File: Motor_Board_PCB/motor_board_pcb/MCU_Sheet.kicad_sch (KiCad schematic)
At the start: 39 parts

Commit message: Motor Board Initial Layout
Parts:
- removed SW?: SW_Push, Button_Switch_SMD:SW_Push_1P1T_NO_6x6mm_H9.5mm, symbol Switch:SW_Push
- removed TP? (x3): TestPoint, TestPoint:TestPoint_Pad_D1.0mm, symbol Connector:TestPoint
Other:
- moved on the sheet: TP?

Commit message: Meeting layout updates
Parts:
- added R7 (x3): 0, Resistor_SMD:R_0402_1005Metric, symbol Device:R
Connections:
- net D10: now also R7.1; no longer U?.37 (GTIOC3B/P112)
- net D11: now also R7.1; no longer U?.34 (CTX0/TDO/SWO/GTIOC1A/P109)
- net D13: now also R7.1; no longer U?.36 (GTIOC3A/P111)
- new net: R7.2, U?.34 (CTX0/TDO/SWO/GTIOC1A/P109)
- new net: R7.2, U?.36 (GTIOC3A/P111)
- new net: R7.2, U?.37 (GTIOC3B/P112)
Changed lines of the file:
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@@
-    (stroke (width 0) (type default))
-  )
-  (wire (pts (xy 190.5 87.63) (xy 208.28 87.63))
     (stroke (width 0) (type default))
   )
@@
     (stroke (width 0) (type default))
   )
+  (wire (pts (xy 198.12 92.71) (xy 215.9 92.71))
+    (stroke (width 0) (type default))
+  )
   (wire (pts (xy 115.57 74.93) (xy 119.38 74.93))
     (stroke (width 0) (type default))
@@
     (stroke (width 0) (type default))
   )
-  (wire (pts (xy 190.5 90.17) (xy 208.28 90.17))
+  (wire (pts (xy 198.12 85.09) (xy 215.9 85.09))
     (stroke (width 0) (type default))
   )
@@
     (stroke (width 0) (type default))
   )
-  (wire (pts (xy 190.5 85.09) (xy 208.28 85.09))
-    (stroke (width 0) (type default))
-  )
   (wire (pts (xy 233.68 102.87) (xy 237.49 102.87))
     (stroke (width 0) (type default))
@@
     (stroke (width 0) (type default))
   )
+  (wire (pts (xy 198.12 90.17) (xy 215.9 90.17))
+    (stroke (width 0) (type default))
+  )
   (wire (pts (xy 119.38 49.53) (xy 105.41 49.53))
     (stroke (width 0) (type default))
@@
     (stroke (width 0) (type default))
   )
-  (wire (pts (xy 190.5 92.71) (xy 208.28 92.71))
-    (stroke (width 0) (type default))
-  )
   (wire (pts (xy 165.1 168.91) (xy 165.1 166.37))
     (stroke (width 0) (type default))
   )
   (wire (pts (xy 73.66 96.52) (xy 73.66 97.79))
+    (stroke (width 0) (type default))
+  )
+  (wire (pts (xy 190.5 87.63) (xy 215.9 87.63))
     (stroke (width 0) (type default))
   )
@@
     (effects (font (size 1.27 1.27)) (justify left bottom))
   )
-  (label "P109_SCI9_TXD" (at 191.77 85.09 0) (fields_autoplaced)
+  (label "P109_SCI9_TXD" (at 201.93 85.09 0) (fields_autoplaced)
     (effects (font (size 1.27 1.27)) (justify left bottom))
   )
@@
     (effects (font (size 1.27 1.27)) (justify left bottom))
   )
-  (label "P111_GPT3_A" (at 191.77 90.17 0) (fields_autoplaced)
+  (label "P111_GPT3_A" (at 201.93 90.17 0) (fields_autoplaced)
     (effects (font (size 1.27 1.27)) (justify left bottom))
   )
@@
     (effects (font (size 1.27 1.27)) (justify left bottom))
   )
-  (label "P112_GPT3_B" (at 191.77 92.71 0) (fields_autoplaced)
+  (label "P112_GPT3_B" (at 201.93 92.71 0) (fields_autoplaced)
     (effects (font (size 1.27 1.27)) (justify left bottom))
   )
@@
     (effects (font (size 1.27 1.27)) (justify left bottom))
   )
-  (label "P110_SCI9_RXD" (at 191.77 87.63 0) (fields_autoplaced)
+  (label "P110_SCI9_RXD" (at 201.93 87.63 0) (fields_autoplaced)
     (effects (font (size 1.27 1.27)) (justify left bottom))
   )
@@
     )
   )
-  (global_label "D11" (shape input) (at 208.28 85.09 0) (fields_autoplaced)
+  (global_label "D11" (shape input) (at 215.9 85.09 0) (fields_autoplaced)
     (effects (font (size 1.27 1.27)) (justify left))
-    (property "Intersheetrefs" "${INTERSHEET_REFS}" (at 214.9542 85.09 0)
+    (property "Intersheetrefs" "${INTERSHEET_REFS}" (at 222.5742 85.09 0)
       (effects (font (size 1.27 1.27)) (justify left) hide)
     )
@@
     )
   )
-  (global_label "D13" (shape input) (at 208.28 90.17 0) (fields_autoplaced)
+  (global_label "D13" (shape input) (at 215.9 90.17 0) (fields_autoplaced)
     (effects (font (size 1.27 1.27)) (justify left))
-    (property "Intersheetrefs" "${INTERSHEET_REFS}" (at 214.9542 90.17 0)
+    (property "Intersheetrefs" "${INTERSHEET_REFS}" (at 222.5742 90.17 0)
       (effects (font (size 1.27 1.27)) (justify left) hide)
     )
@@
     )
   )
-  (global_label "D10" (shape input) (at 208.28 92.71 0) (fields_autoplaced)
+  (global_label "D10" (shape input) (at 215.9 92.71 0) (fields_autoplaced)
     (effects (font (size 1.27 1.27)) (justify left))
-    (property "Intersheetrefs" "${INTERSHEET_REFS}" (at 214.9542 92.71 0)
+    (property "Intersheetrefs" "${INTERSHEET_REFS}" (at 222.5742 92.71 0)
       (effects (font (size 1.27 1.27)) (justify left) hide)
     )
@@
     )
   )
-  (global_label "D12" (shape input) (at 208.28 87.63 0) (fields_autoplaced)
+  (global_label "D12" (shape input) (at 215.9 87.63 0) (fields_autoplaced)
     (effects (font (size 1.27 1.27)) (justify left))
-    (property "Intersheetrefs" "${INTERSHEET_REFS}" (at 214.9542 87.63 0)
+    (property "Intersheetrefs" "${INTERSHEET_REFS}" (at 222.5742 87.63 0)
       (effects (font (size 1.27 1.27)) (justify left) hide)
     )
@@
         (path "/4ad82a24-c992-45c9-b523-12e12bcd6ced/677bf49c-46b9-40dd-b186-394fb8d84e12"
           (reference "#PWR019") (unit 1)
+        )
+      )
+    )
+  )
+  (symbol (lib_id "Device:R") (at 194.31 85.09 270) (unit 1)
+    (in_bom yes) (on_board yes) (dnp no)
+    (property "Reference" "R7" (at 199.39 86.36 90)
+      (effects (font (size 1.27 1.27)))
+    )
+    (property "Value" "0" (at 190.5 83.82 90)
+      (effects (font (size 1.27 1.27)))
+    )
+    (property "Footprint" "Resistor_SMD:R_0402_1005Metric" (at 194.31 83.312 90)
+      (effects (font (size 1.27 1.27)) hide)
+    )
+    (property "Datasheet" "~" (at 194.31 85.09 0)
+      (effects (font (size 1.27 1.27)) hide)
+    )
+    (pin "1")
+    (pin "2")
+    (instances
+      (project "central_hub"
+        (path "/0d9ec66e-0fbf-4d12-9b83-adf78971a00b/a9a7affa-d8a7-4dcd-8fe3-0de6a2b29bd6"
+          (reference "R7") (unit 1)
+        )
+        (path "/0d9ec66e-0fbf-4d12-9b83-adf78971a00b/4fb60496-ee10-4e45-a75e-a49c2c8afc68"
+          (reference "R35") (unit 1)
+        )
+      )
+      (project "motor_board_pcb"
+        (path "/4ad82a24-c992-45c9-b523-12e12bcd6ced"
+          (reference "R?") (unit 1)
+        )
+        (path "/4ad82a24-c992-45c9-b523-12e12bcd6ced/63c66207-e5d4-4f6f-af8f-451675dc3930"
+          (reference "R16") (unit 1)
+        )
+        (path "/4ad82a24-c992-45c9-b523-12e12bcd6ced/677bf49c-46b9-40dd-b186-394fb8d84e12"
+          (reference "R7") (unit 1)
         )
       )
@@
     )
   )
+  (symbol (lib_id "Device:R") (at 194.31 92.71 270) (unit 1)
+    (in_bom yes) (on_board yes) (dnp no)
+    (property "Reference" "R7" (at 199.39 93.98 90)
+      (effects (font (size 1.27 1.27)))
+    )
+    (property "Value" "0" (at 190.5 91.44 90)
+      (effects (font (size 1.27 1.27)))
+    )
+    (property "Footprint" "Resistor_SMD:R_0402_1005Metric" (at 194.31 90.932 90)
+      (effects (font (size 1.27 1.27)) hide)
+    )
+    (property "Datasheet" "~" (at 194.31 92.71 0)
+      (effects (font (size 1.27 1.27)) hide)
+    )
+    (pin "1")
+    (pin "2")
+    (instances
+      (project "central_hub"
+        (path "/0d9ec66e-0fbf-4d12-9b83-adf78971a00b/a9a7affa-d8a7-4dcd-8fe3-0de6a2b29bd6"
+          (reference "R7") (unit 1)
+        )
+        (path "/0d9ec66e-0fbf-4d12-9b83-adf78971a00b/4fb60496-ee10-4e45-a75e-a49c2c8afc68"
+          (reference "R35") (unit 1)
+        )
+      )
+      (project "motor_board_pcb"
+        (path "/4ad82a24-c992-45c9-b523-12e12bcd6ced"
+          (reference "R?") (unit 1)
+        )
+        (path "/4ad82a24-c992-45c9-b523-12e12bcd6ced/63c66207-e5d4-4f6f-af8f-451675dc3930"
+          (reference "R16") (unit 1)
+        )
+        (path "/4ad82a24-c992-45c9-b523-12e12bcd6ced/677bf49c-46b9-40dd-b186-394fb8d84e12"
+          (reference "R35") (unit 1)
+        )
+      )
+    )
+  )
   (symbol (lib_id "Device:C") (at 80.01 52.07 90) (unit 1)
     (in_bom yes) (on_board yes) (dnp no) (fields_autoplaced)
@@
         )
       )
+    )
+  )
+  (symbol (lib_id "Device:R") (at 194.31 90.17 270) (unit 1)
+    (in_bom yes) (on_board yes) (dnp no)
+    (property "Reference" "R7" (at 199.39 91.44 90)
+      (effects (font (size 1.27 1.27)))
+    )
+    (property "Value" "0" (at 190.5 88.9 90)
+      (effects (font (size 1.27 1.27)))
+    )
+    (property "Footprint" "Resistor_SMD:R_0402_1005Metric" (at 194.31 88.392 90)
+      (effects (font (size 1.27 1.27)) hide)
+    )
+    (property "Datasheet" "~" (at 194.31 90.17 0)
+      (effects (font (size 1.27 1.27)) hide)
+    )
+    (pin "1")
+    (pin "2")
+    (instances
+      (project "central_hub"
+        (path "/0d9ec66e-0fbf-4d12-9b83-adf78971a00b/a9a7affa-d8a7-4dcd-8fe3-0de6a2b29bd6"
+          (reference "R7") (unit 1)
+        )
+        (path "/0d9ec66e-0fbf-4d12-9b83-adf78971a00b/4fb60496-ee10-4e45-a75e-a49c2c8afc68"
+          (reference "R35") (unit 1)
+        )
+      )
+      (project "motor_board_pcb"
+        (path "/4ad82a24-c992-45c9-b523-12e12bcd6ced"
+          (reference "R?") (unit 1)
+        )
+        (path "/4ad82a24-c992-45c9-b523-12e12bcd6ced/63c66207-e5d4-4f6f-af8f-451675dc3930"
+          (reference "R16") (unit 1)
+        )
+        (path "/4ad82a24-c992-45c9-b523-12e12bcd6ced/677bf49c-46b9-40dd-b186-394fb8d84e12"
+          (reference "R34") (unit 1)
+        )
+      )

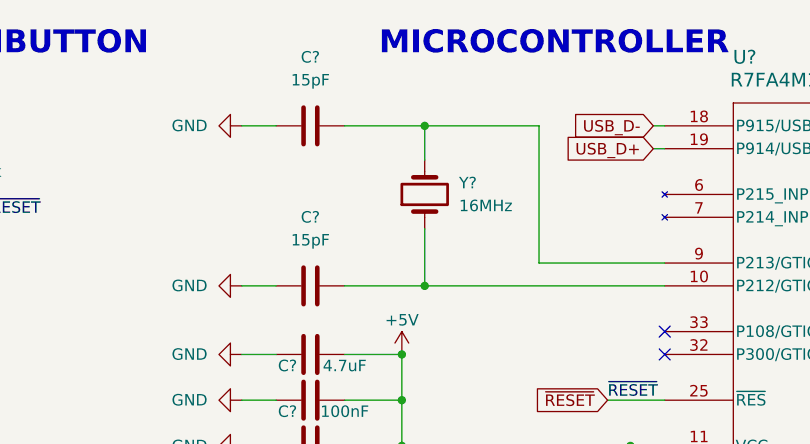
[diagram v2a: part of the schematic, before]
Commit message: Kim changes + GND pour + TearDrops + Oscillator changes
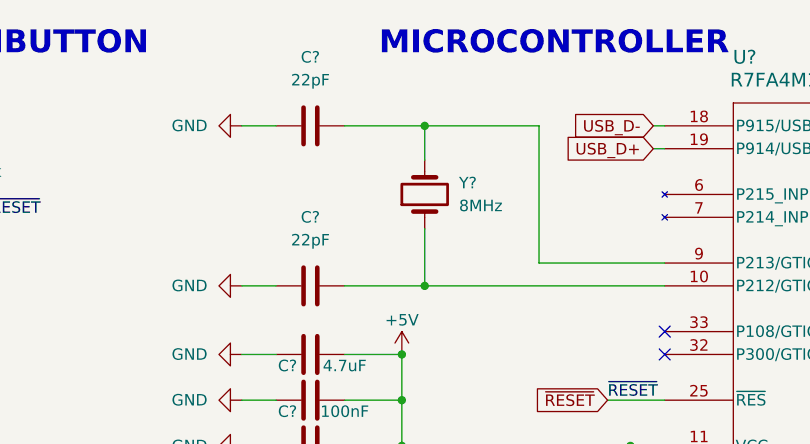
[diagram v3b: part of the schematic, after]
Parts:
- C? (x2): value 15pF -> 22pF
- Y?: value 16MHz -> 8MHz
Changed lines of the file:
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@@
       (effects (font (size 1.27 1.27)))
     )
-    (property "Value" "15pF" (at 80.01 29.21 90)
+    (property "Value" "22pF" (at 80.01 29.21 90)
       (effects (font (size 1.27 1.27)))
     )
@@
       (effects (font (size 1.27 1.27)) (justify right))
     )
-    (property "Value" "16MHz" (at 96.52 43.18 90)
+    (property "Value" "8MHz" (at 96.52 43.18 90)
       (effects (font (size 1.27 1.27)) (justify right))
     )
@@
       (effects (font (size 1.27 1.27)))
     )
-    (property "Value" "15pF" (at 80.01 46.99 90)
-      (effects (font (size 1.27 1.27)))
-    )
+    (property "Value" "22pF" (at 80.01 46.99 90)
+      (effects (font (size 1.27 1.27)))
+    )

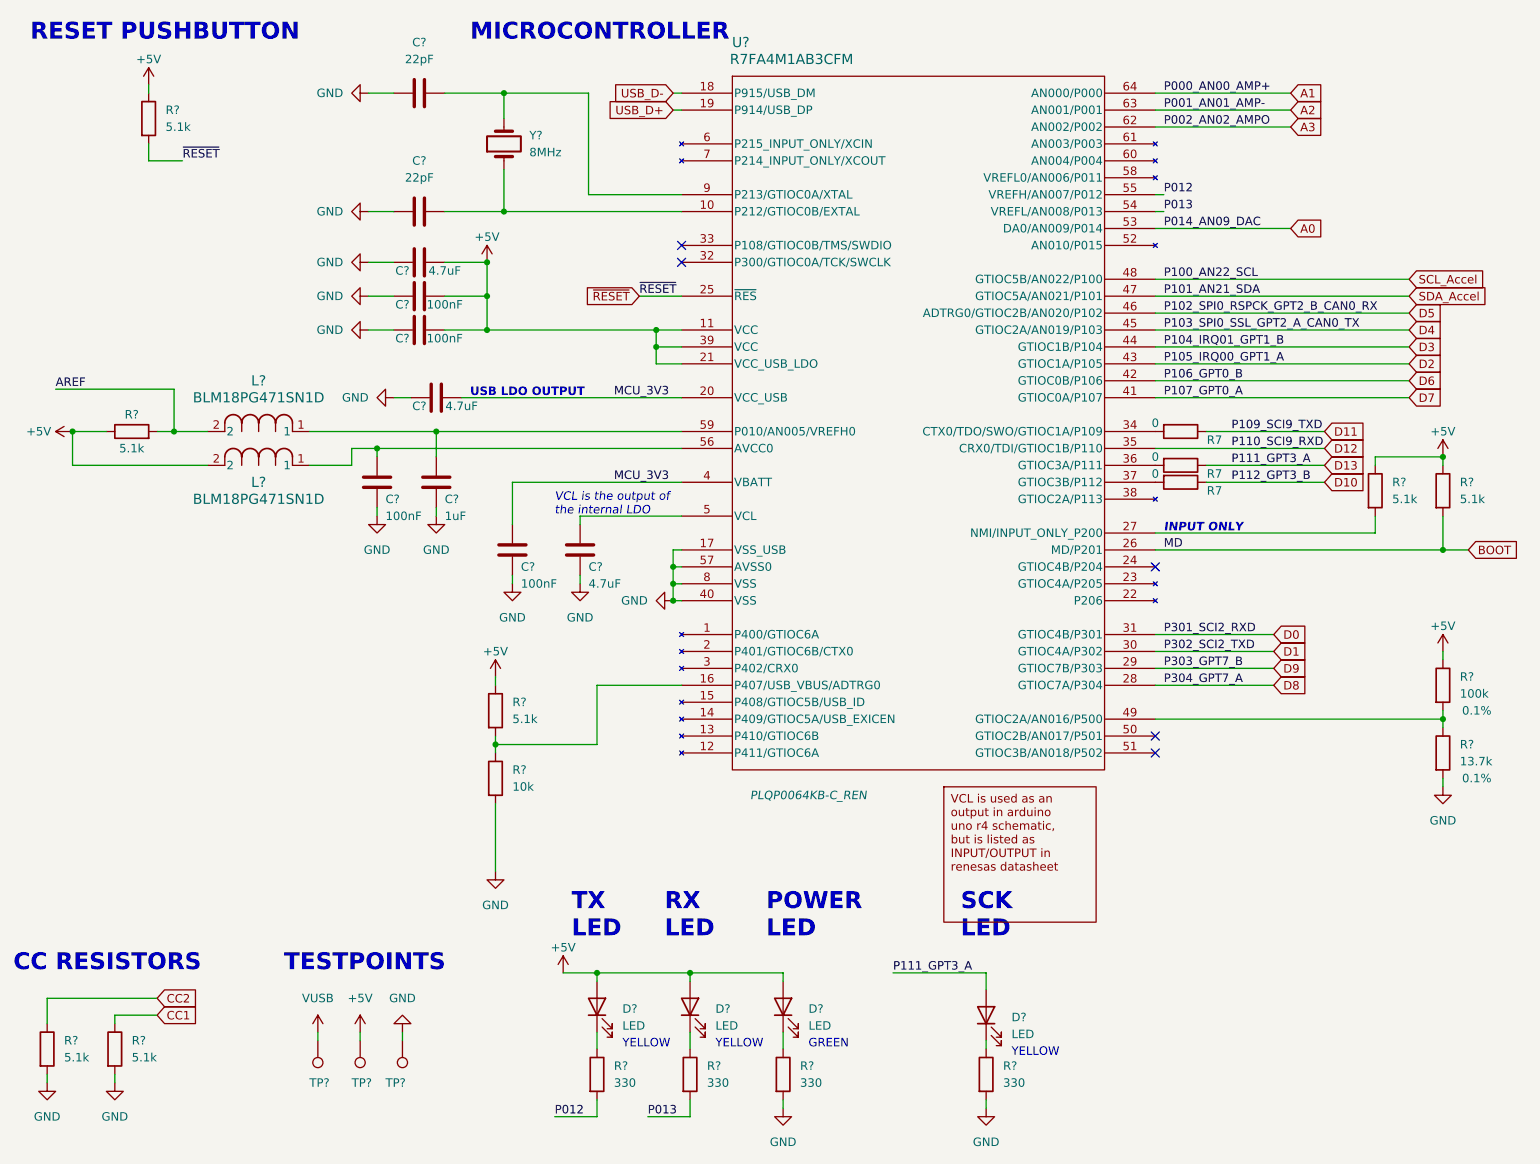
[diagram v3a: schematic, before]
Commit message: - added footprint labels to schematic symbols
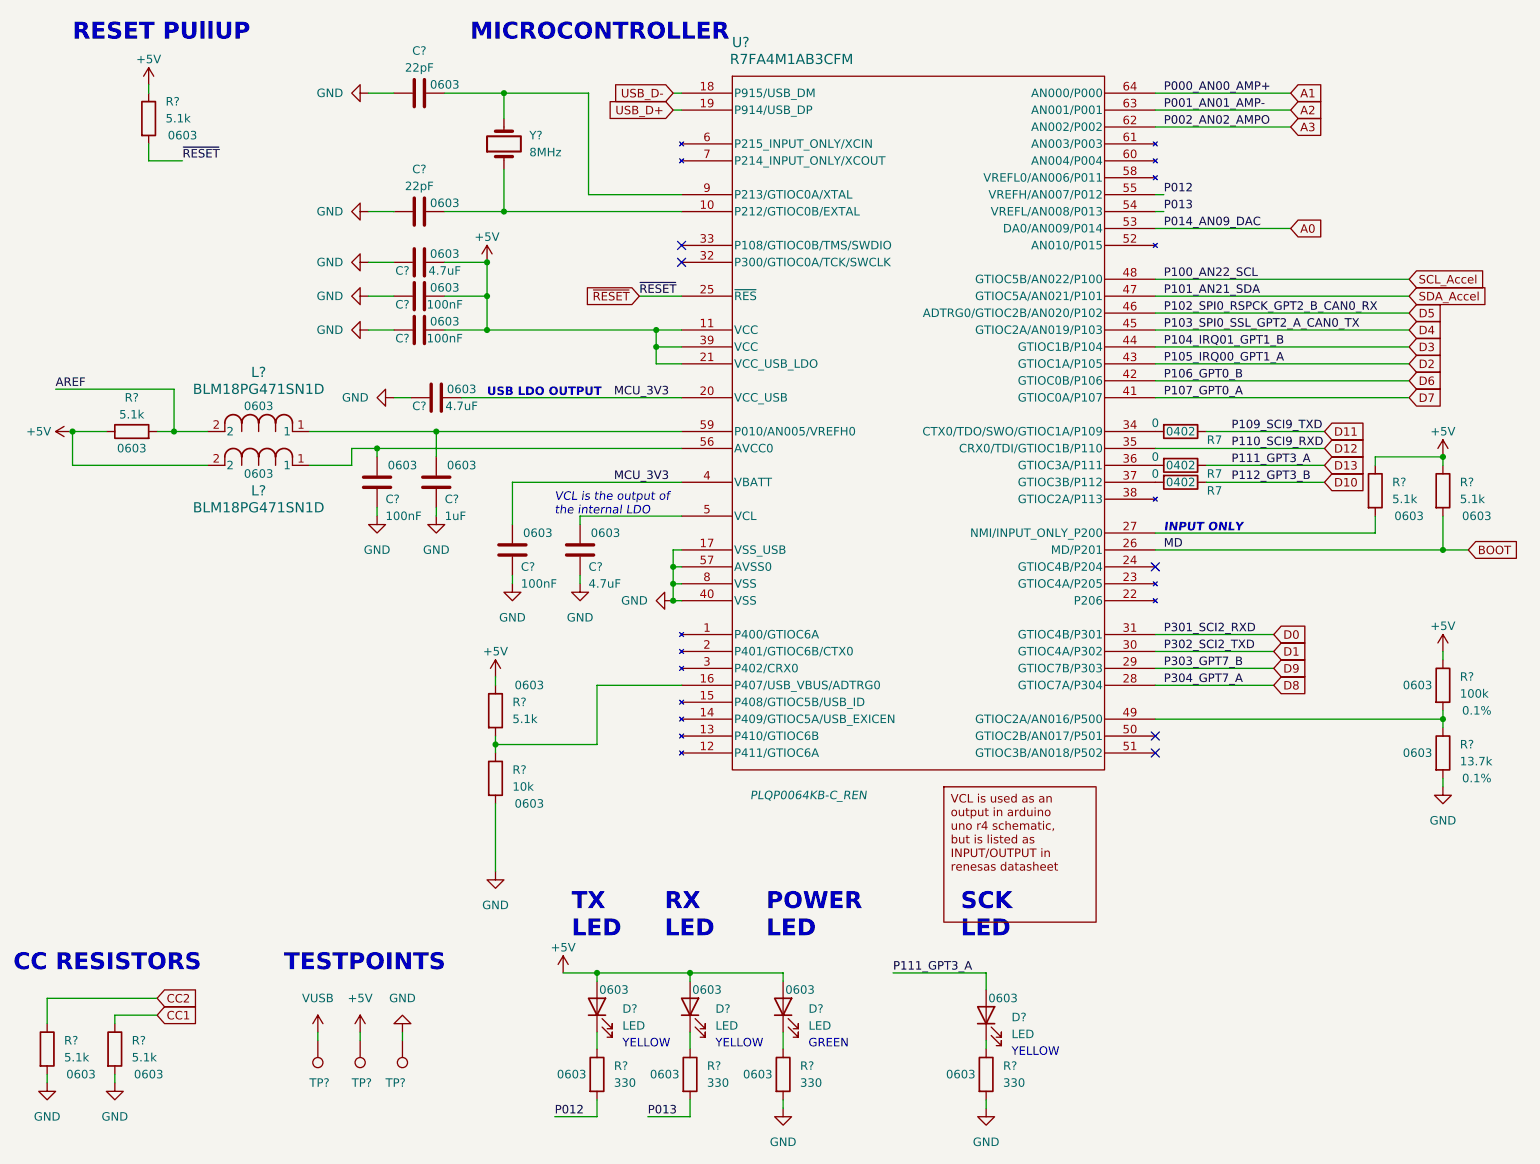
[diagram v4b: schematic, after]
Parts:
- C? (x10), D? (x4), L? (x2), R? (x14): FP (none) -> 0603
- R7: FP (none) -> 0402
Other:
- note added: "RESET PUllUP"
- note removed: "RESET PUSHBUTTON"
